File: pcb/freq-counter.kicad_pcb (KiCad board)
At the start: 4 copper layers, 152.4 x 195.6 mm, 103 parts, among them J1 RPM on board, J10 Power_T1, J2 BNC, J3 RPM to Board, J4 Jack-DC, J5 Segments-Terminal0, J6 Digits-Terminal0, J7 Segments-Terminal1, J8 Digits-Terminal1, J9 Power_Terminal1, Q1 CSC388A, Q10 2SC1815, Q11 2SC1815, Q12 2SC1815, Q13 2SC1815, Q14 2SC1815, Q2 CSC388A, Q3 2SA1015, Q4 2SC1815, Q5 2SC1815, Q6 CSC388A, Q7 CSC388A, Q8 CSC388A, Q9 2SC1815, SW1 on/off, SW2 count up, SW3 toggle, SW4 SW_SIGNAL, U1 SN74HC02N, U2 ATTINY4313-PU(freq-counter), U3 EE-SX460, U4 74HC00, U5 74HC00, U6 74HC00, U7 7seg-2digit-ca, U8 7seg-2digit-ca, U9 7seg-2digit-ca, Y1 10MHz

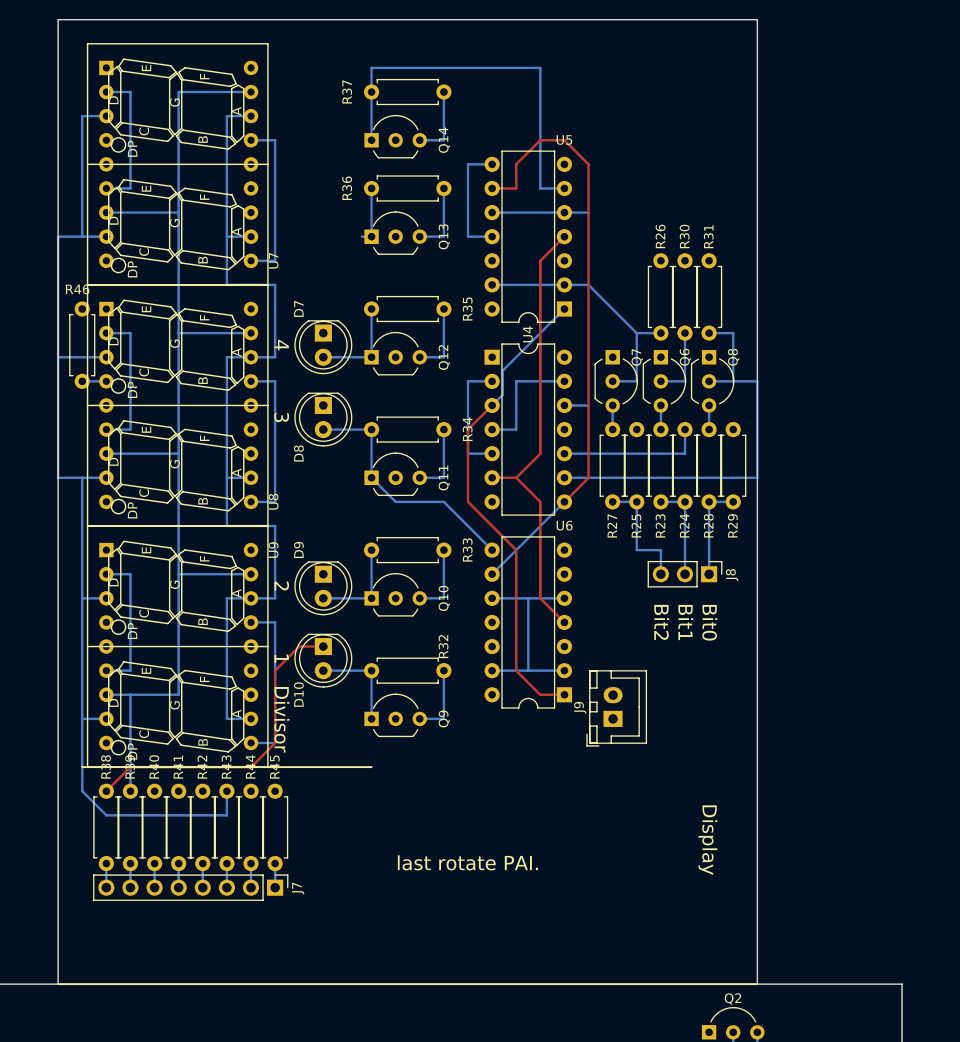
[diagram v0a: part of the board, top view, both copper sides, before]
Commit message: Display 部を決定。これに合わせて母板を設計する。
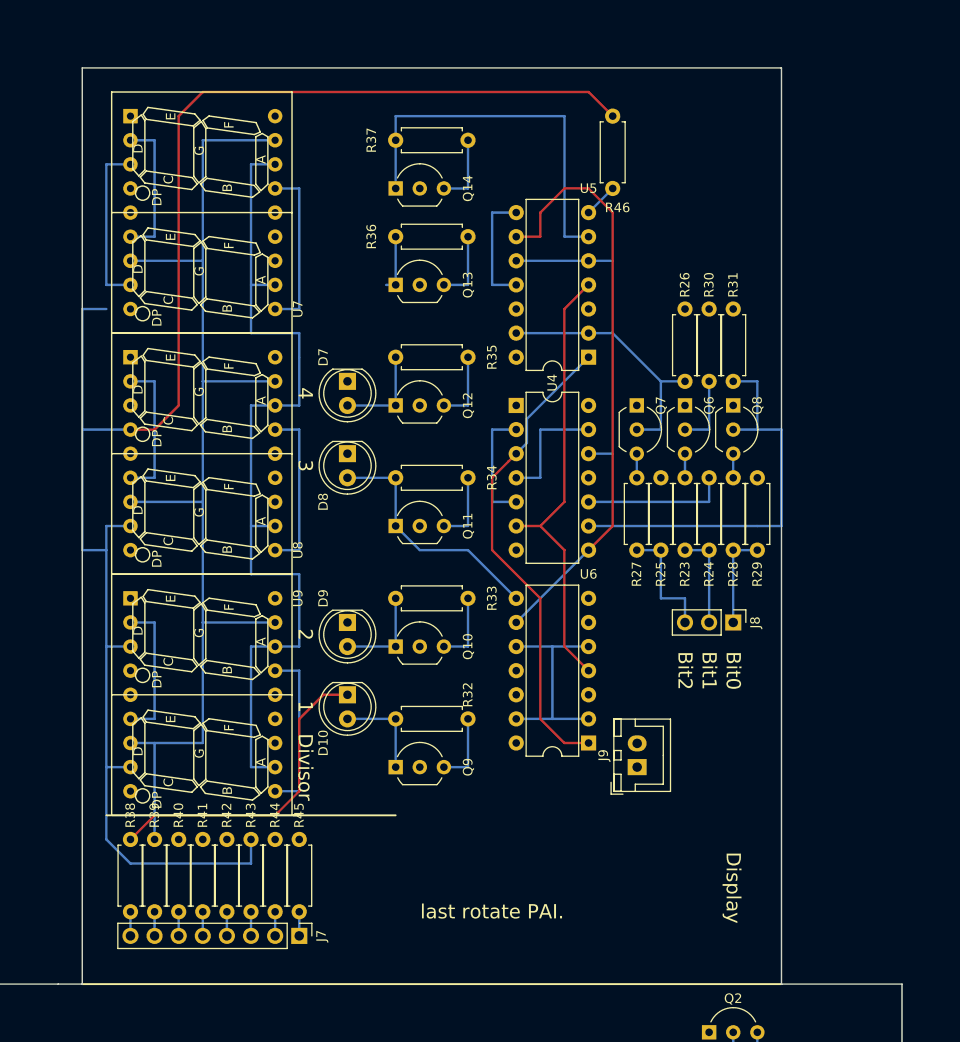
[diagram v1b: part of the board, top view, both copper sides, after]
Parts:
- moved R46 57.3 mm to (149.9, 20.3), turned to 90 degrees
- moved R24 5.68 mm to (160.0, 58.4)
- moved R38 5.68 mm to (99.1, 88.9)
- moved R40 5.68 mm to (104.1, 88.9)
- moved R42 5.68 mm to (109.2, 88.9)
- moved R44 5.68 mm to (114.3, 88.9)
- moved R45 5.68 mm to (116.8, 88.9)
- moved D8 5.68 mm to (121.9, 48.3)
- moved Q10 5.68 mm to (127.0, 68.6)
- moved R30 5.68 mm to (160.0, 40.6)
- moved R32 5.68 mm to (134.6, 76.2)
- moved R39 5.68 mm to (101.6, 88.9)
- moved R41 5.68 mm to (106.7, 88.9)
- moved R43 5.68 mm to (111.8, 88.9)
- moved Q13 5.68 mm to (127.0, 30.5)
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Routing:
- net GND_T1: track 192.8 -> 105.0 mm
- net Net-(R46-Pad2): track 2.54 -> 84.4 mm
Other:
- board size 152.4 x 195.6 mm -> 152.4 x 190.5 mm

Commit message: Display板の大きさ，向きが決まった。Displayに合わせて母板を仕上げる。
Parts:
- moved U7 69.1 mm to (99.1, 91.6), turned to 0 degrees
- moved R38 66.8 mm to (165.1, 99.1), turned to 0 degrees
- moved R37 64.8 mm to (91.4, 63.5), turned to 270 degrees
- moved R39 64.0 mm to (165.1, 96.5), turned to 0 degrees
- moved R40 61.2 mm to (165.1, 94.0), turned to 0 degrees
- moved J7 61.1 mm to (175.3, 81.3), turned to 0 degrees
- moved R46 60.2 mm to (96.5, 48.3), turned to 180 degrees
- moved Q14 59.2 mm to (96.5, 71.1), turned to 90 degrees
- moved R41 58.5 mm to (165.1, 91.4), turned to 0 degrees
- moved R42 55.9 mm to (165.1, 88.9), turned to 0 degrees
- moved R43 53.4 mm to (165.1, 86.4), turned to 0 degrees
- moved R44 51.1 mm to (165.1, 83.8), turned to 0 degrees
- moved R36 50.4 mm to (101.6, 63.5), turned to 270 degrees
- moved R45 48.9 mm to (165.1, 81.3), turned to 0 degrees
- moved U9 46.9 mm to (149.9, 91.6), turned to 0 degrees
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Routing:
- net /7seg/KC: track 113.3 -> 105.7 mm
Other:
- board size 152.4 x 190.5 mm -> 152.4 x 167.6 mm
- board text removed: "last rotate PAI."

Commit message: Display部に，Hz/RPM用のLEDとPUSH-BUTTONを移動させた。Display部は，本当に完成。
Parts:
- moved J2 148.7 mm to (-30.5, 208.3)
- moved C9 138.0 mm to (-71.1, 162.6)
- moved Q1 138.0 mm to (20.3, 162.6)
- moved R12 138.0 mm to (-5.08, 172.7)
- moved R18 138.0 mm to (-71.1, 172.7)
- moved R2 138.0 mm to (30.5, 132.1)
- moved R7 138.0 mm to (30.5, 142.2)
- moved C1 138.0 mm to (35.6, 147.3)
- moved C2 138.0 mm to (40.6, 147.3)
- moved C3 138.0 mm to (-45.7, 172.7)
- moved C4 138.0 mm to (-43.2, 172.8)
- moved C5 138.0 mm to (-33.0, 193.0)
- moved C6 138.0 mm to (-30.5, 193.0)
- moved C7 138.0 mm to (-83.8, 162.6)
- moved C8 138.0 mm to (-12.7, 170.2)
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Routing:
- net Net-(R46-Pad2): track 84.4 -> 60.5 mm
- net GND_T1: track 105.0 -> 119.3 mm
- net /KD15: track 54.4 -> 44.0 mm
- net Net-(R11-Pad1): track 5.13 -> 2.54 mm
- net Net-(D1-Pad1): track 35.6 -> 33.0 mm
- net Net-(Q14-Pad3): track 7.62 -> 6.13 mm

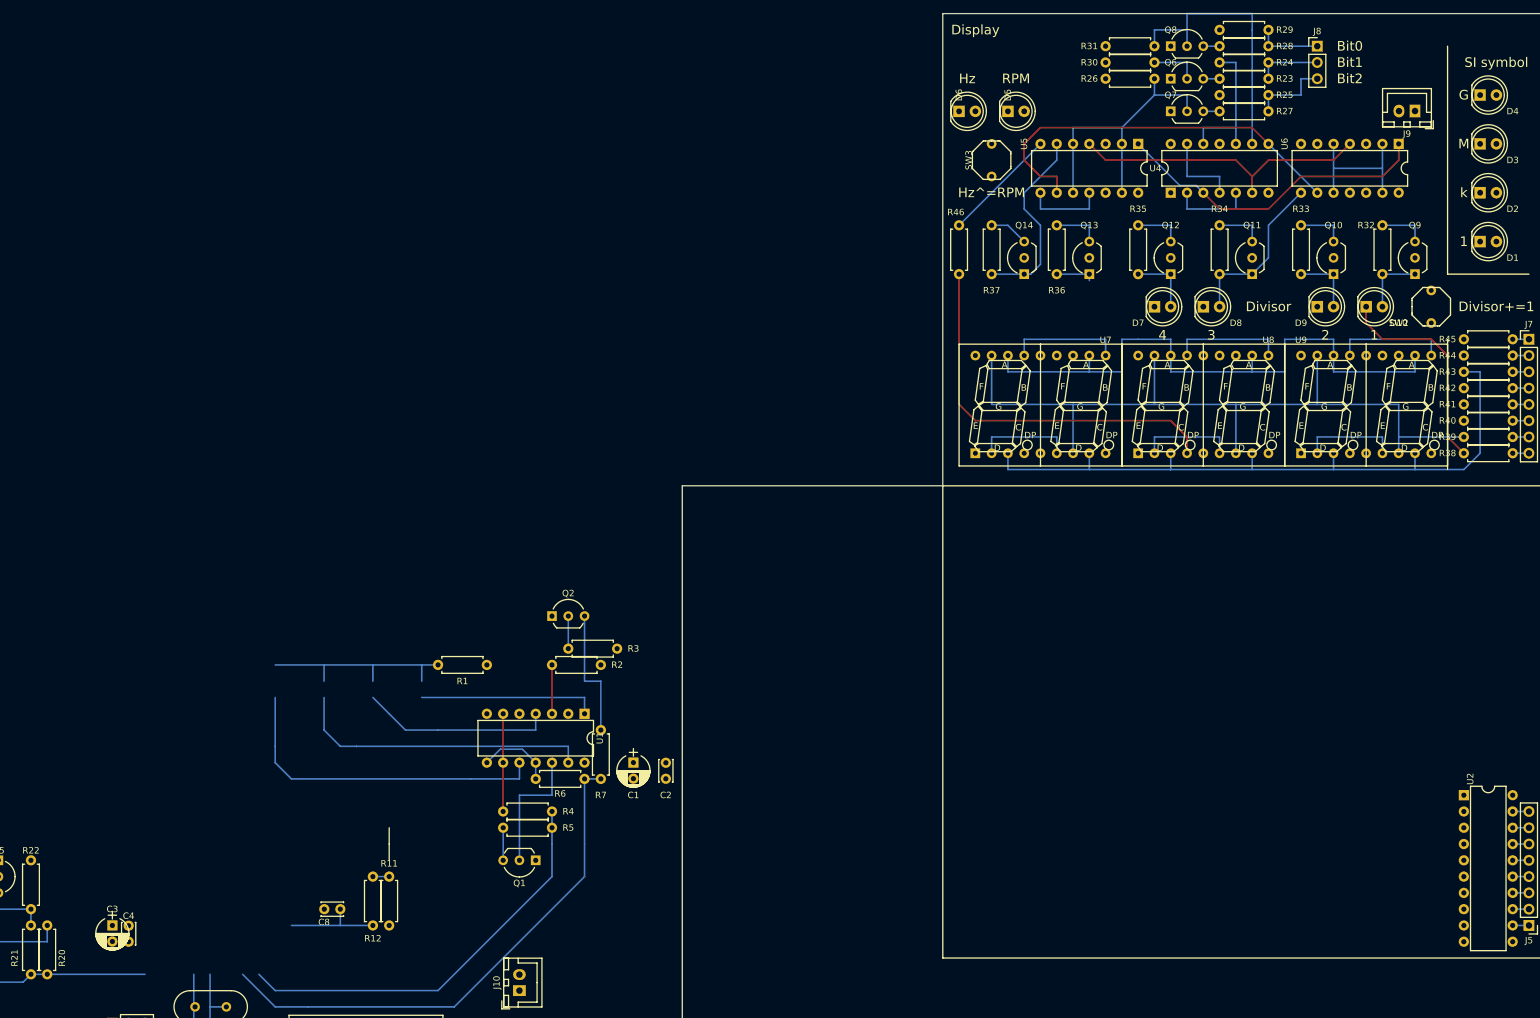
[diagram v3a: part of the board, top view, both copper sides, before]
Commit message: Display 部にLED用の電流制限抵抗を移動させた。Display部のtestをしやすくするため。
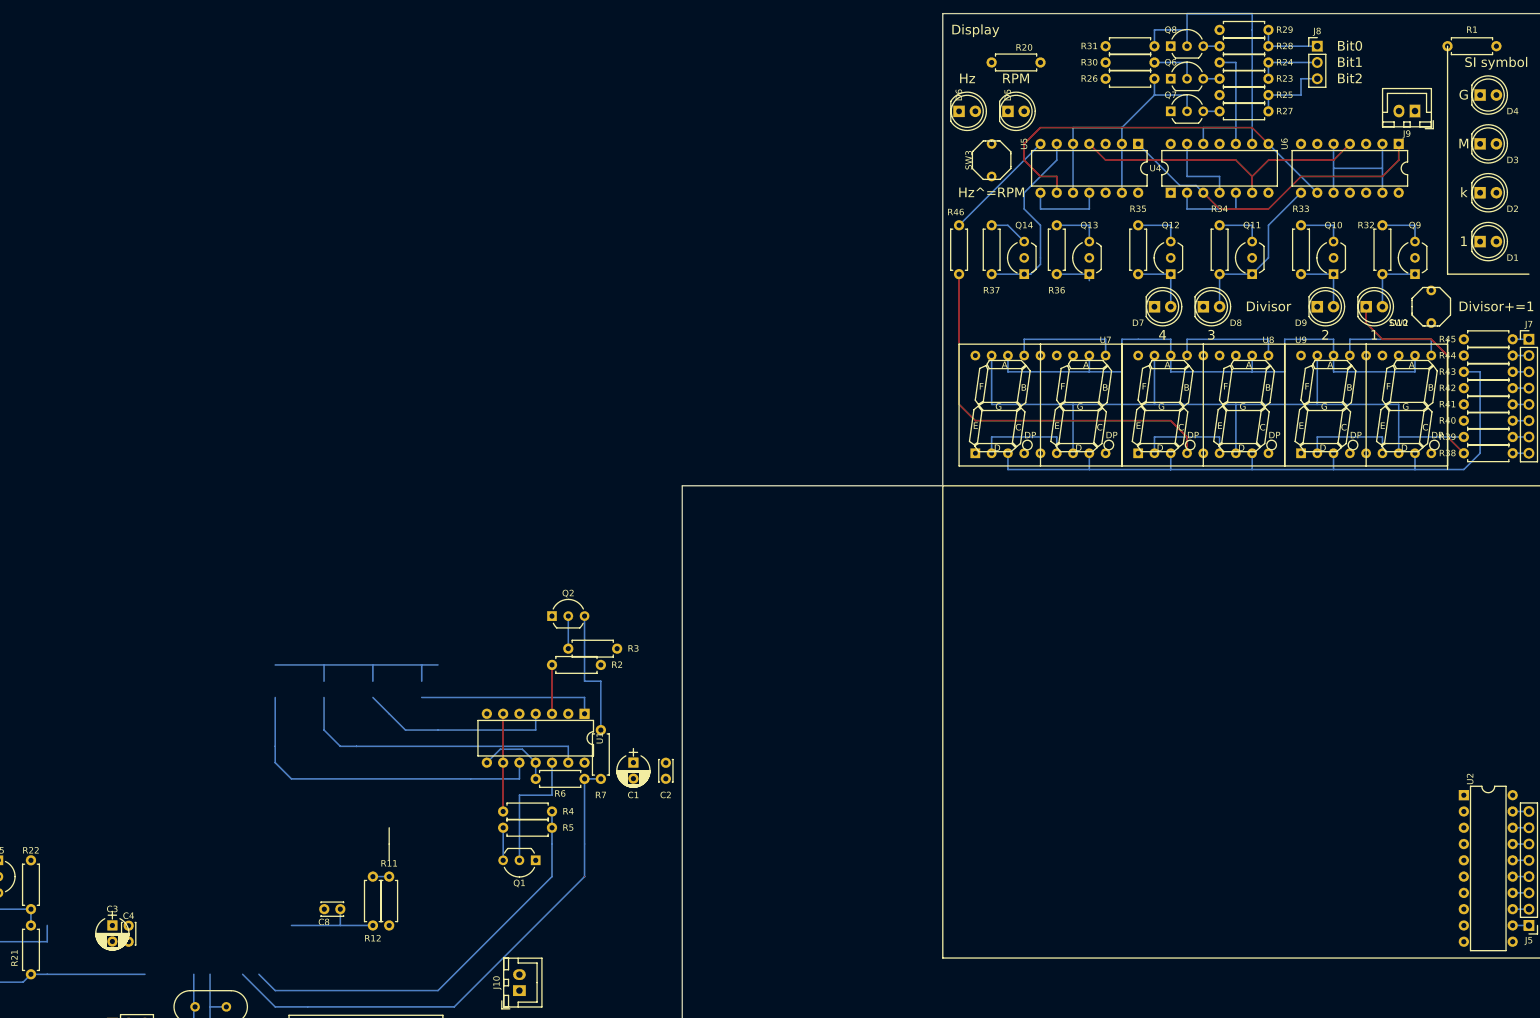
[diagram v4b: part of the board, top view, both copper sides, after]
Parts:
- moved R20 199.6 mm to (91.4, 38.1), turned to 0 degrees
- moved R1 191.2 mm to (170.2, 35.6), turned to 180 degrees
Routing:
- net (no net): track 12.7 -> 17.8 mm
- net Net-(D1-Pad1): track 33.0 -> 27.9 mm
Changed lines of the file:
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@@
   (general
     (links 253)
-    (no_connects 71)
+    (no_connects 81)
     (area 43.104999 30.40317 195.655012 198.195006)
     (thickness 1.6)
@@
   )
   (module Resistors_THT:R_Axial_DIN0207_L6.3mm_D2.5mm_P7.62mm_Horizontal (layer F.Cu)
-    (at 5.08 132.08)
+    (at 170.18 35.56 180)
     (descr "Resistor, Axial_DIN0207 series, Axial, Horizontal, pin pitch=7.62mm, 0.25W = 1/4W, length*diameter=6.3*2.5mm^2, http://cdn-reichelt.de/documents/datenblatt/B400/1_4W%23YAG.pdf")
     (tags "Resistor Axial_DIN0207 series Axial Horizontal pin pitch 7.62mm 0.25W = 1/4W length 6.3mm diameter 2.5mm")
-    (fp_text reference R1 (at 3.809998 2.540007) (layer F.SilkS)
+    (fp_text reference R1 (at 3.809998 2.540007 180) (layer F.SilkS)
       (effects (font (size 1 1) (thickness 0.15)))
     )
-    (fp_text value 470 (at 3.809998 0.000007) (layer F.Fab)
+    (fp_text value 470 (at 3.809998 0.000007 180) (layer F.Fab)
       (effects (font (size 1 1) (thickness 0.15)))
     )
@@
     (fp_line (start 8.7 1.6) (end 8.7 -1.6) (layer F.CrtYd) (width 0.05))
     (fp_line (start 8.7 -1.6) (end -1.05 -1.6) (layer F.CrtYd) (width 0.05))
-    (pad 1 thru_hole circle (at 0 0) (size 1.6 1.6) (drill 0.8) (layers *.Cu *.Mask)
+    (pad 1 thru_hole circle (at 0 0 180) (size 1.6 1.6) (drill 0.8) (layers *.Cu *.Mask)
       (net 6 "Net-(D1-Pad1)"))
-    (pad 2 thru_hole oval (at 7.62 0) (size 1.6 1.6) (drill 0.8) (layers *.Cu *.Mask)
+    (pad 2 thru_hole oval (at 7.62 0 180) (size 1.6 1.6) (drill 0.8) (layers *.Cu *.Mask)
       (net 95 GND))
     (model ${KISYS3DMOD}/Resistors_THT.3dshapes/R_Axial_DIN0207_L6.3mm_D2.5mm_P7.62mm_Horizontal.wrl
@@
   )
   (module Resistors_THT:R_Axial_DIN0207_L6.3mm_D2.5mm_P7.62mm_Horizontal (layer F.Cu)
-    (at -55.879994 172.719995 270)
+    (at 91.44 38.1)
     (descr "Resistor, Axial_DIN0207 series, Axial, Horizontal, pin pitch=7.62mm, 0.25W = 1/4W, length*diameter=6.3*2.5mm^2, http://cdn-reichelt.de/documents/datenblatt/B400/1_4W%23YAG.pdf")
     (tags "Resistor Axial_DIN0207 series Axial Horizontal pin pitch 7.62mm 0.25W = 1/4W length 6.3mm diameter 2.5mm")
-    (fp_text reference R20 (at 5.080005 -2.31 270) (layer F.SilkS)
+    (fp_text reference R20 (at 5.080005 -2.31) (layer F.SilkS)
       (effects (font (size 1 1) (thickness 0.15)))
     )
-    (fp_text value 470 (at 3.81 0.000006 270) (layer F.Fab)
+    (fp_text value 470 (at 3.81 0.000006) (layer F.Fab)
       (effects (font (size 1 1) (thickness 0.15)))
     )
@@
     (fp_line (start 8.7 1.6) (end 8.7 -1.6) (layer F.CrtYd) (width 0.05))
     (fp_line (start 8.7 -1.6) (end -1.05 -1.6) (layer F.CrtYd) (width 0.05))
-    (pad 1 thru_hole circle (at 0 0 270) (size 1.6 1.6) (drill 0.8) (layers *.Cu *.Mask)
+    (pad 1 thru_hole circle (at 0 0) (size 1.6 1.6) (drill 0.8) (layers *.Cu *.Mask)
       (net 11 "Net-(D5-Pad1)"))
-    (pad 2 thru_hole oval (at 7.62 0 270) (size 1.6 1.6) (drill 0.8) (layers *.Cu *.Mask)
+    (pad 2 thru_hole oval (at 7.62 0) (size 1.6 1.6) (drill 0.8) (layers *.Cu *.Mask)
       (net 22 /Hz/RPM))
     (model ${KISYS3DMOD}/Resistors_THT.3dshapes/R_Axial_DIN0207_L6.3mm_D2.5mm_P7.62mm_Horizontal.wrl
@@
   (segment (start 106.679994 60.959984) (end 99.059994 60.959984) (width 0.25) (layer B.Cu) (net 0))
   (segment (start 106.679994 58.419984) (end 106.679994 60.959984) (width 0.25) (layer B.Cu) (net 0))
+  (segment (start -5.08 134.62) (end -5.08 132.08) (width 0.25) (layer B.Cu) (net 0))
+  (segment (start -12.7 134.62) (end -12.7 132.08) (width 0.25) (layer B.Cu) (net 0))
+  (segment (start 27.940002 165.099998) (end 27.94 165.1) (width 0.25) (layer F.Cu) (net 0))
   (segment (start -33.02 190.5) (end -33.02 185.62) (width 0.25) (layer B.Cu) (net 1) (status 30))
   (segment (start -33.02 185.62) (end -33.02 180.34) (width 0.25) (layer B.Cu) (net 1) (status 30))
@@
   (segment (start 2.54 132.08) (end -20.32 132.08) (width 0.25) (layer B.Cu) (net 6))
   (segment (start 2.540002 134.619993) (end 2.540002 132.080002) (width 0.25) (layer B.Cu) (net 6))
-  (segment (start -5.08 134.62) (end -5.08 132.08) (width 0.25) (layer B.Cu) (net 6))
-  (segment (start -12.7 134.62) (end -12.7 132.08) (width 0.25) (layer B.Cu) (net 6))
   (segment (start -17.78 149.86) (end 10.16 149.86) (width 0.25) (layer B.Cu) (net 7))
   (segment (start -20.32 147.32) (end -17.78 149.86) (width 0.25) (layer B.Cu) (net 7))
@@
   (segment (start 27.94 165.1) (end 7.62 185.42) (width 0.25) (layer B.Cu) (net 44))
   (segment (start -25.4 180.34) (end -20.32 185.42) (width 0.25) (layer B.Cu) (net 44) (status 10))
-  (segment (start 27.940002 165.099998) (end 27.94 165.1) (width 0.25) (layer F.Cu) (net 44))
   (segment (start 27.940002 149.859993) (end 27.940002 160.019998) (width 0.25) (layer B.Cu) (net 44) (status 10))
   (segment (start 30.480002 149.859993) (end 27.940002 149.859993) (width 0.25) (layer B.Cu) (net 44) (status 30))
@@
   (segment (start 165.09999 91.439996) (end 167.638165 91.439996) (width 0.25) (layer In1.Cu) (net 58))
   (segment (start 152.399994 101.599984) (end 149.859994 99.059984) (width 0.25) (layer In1.Cu) (net 58))
-  (segment (start 172.719982 91.439996) (end 172.719994 91.440008) (width 0.25) (layer In1.Cu) (net 58))
   (segment (start 88.899994 96.519984) (end 88.899994 99.059984) (width 0.25) (layer In1.Cu) (net 58))
   (segment (start 99.059994 96.519984) (end 88.899994 96.519984) (width 0.25) (layer In1.Cu) (net 58))
@@
   (segment (start 149.859994 99.059984) (end 149.859994 98.932984) (width 0.25) (layer B.Cu) (net 58) (status 30))
   (segment (start 99.059994 99.059984) (end 99.059994 98.932984) (width 0.25) (layer B.Cu) (net 58) (status 30))
+  (segment (start 172.719982 91.439996) (end 172.719994 91.440008) (width 0.25) (layer In1.Cu) (net 59))
   (segment (start 175.260001 91.439996) (end 172.720001 91.439996) (width 0.25) (layer B.Cu) (net 59) (status 30))
   (segment (start 160.019982 88.899996) (end 165.09999 88.899996) (width 0.25) (layer In2.Cu) (net 60))
@@
   (segment (start 167.638165 86.359996) (end 167.63999 86.361821) (width 0.25) (layer B.Cu) (net 62))
   (segment (start 165.09999 86.359996) (end 167.638165 86.359996) (width 0.25) (layer B.Cu) (net 62))
-  (segment (start 172.719982 86.359996) (end 172.719994 86.360008) (width 0.25) (layer B.Cu) (net 62))
   (segment (start 132.079994 101.599984) (end 144.779994 101.599984) (width 0.25) (layer B.Cu) (net 62))
   (segment (start 132.079994 99.059984) (end 132.079994 101.599984) (width 0.25) (layer B.Cu) (net 62))
@@
   (segment (start 144.779994 101.599984) (end 157.479994 101.599984) (width 0.25) (layer B.Cu) (net 62))
   (segment (start 144.779994 98.932984) (end 144.779994 101.599984) (width 0.25) (layer B.Cu) (net 62) (status 10))
+  (segment (start 172.719982 86.359996) (end 172.719994 86.360008) (width 0.25) (layer B.Cu) (net 63))
   (segment (start 175.260001 86.359996) (end 172.720001 86.359996) (width 0.25) (layer B.Cu) (net 63) (status 30))
   (segment (start 96.519994 81.279984) (end 96.519994 83.692984) (width 0.25) (layer B.Cu) (net 64) (status 20))
